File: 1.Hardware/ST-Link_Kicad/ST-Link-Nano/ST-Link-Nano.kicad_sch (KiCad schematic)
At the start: 26 parts, among them J1 USB_C_Receptacle_USB2.0, J2 JUMP, J3 Conn_02x04_Top_Bottom, U1 XC6210B332MR, U2 STM32F103CBTx, Y1 8MHz

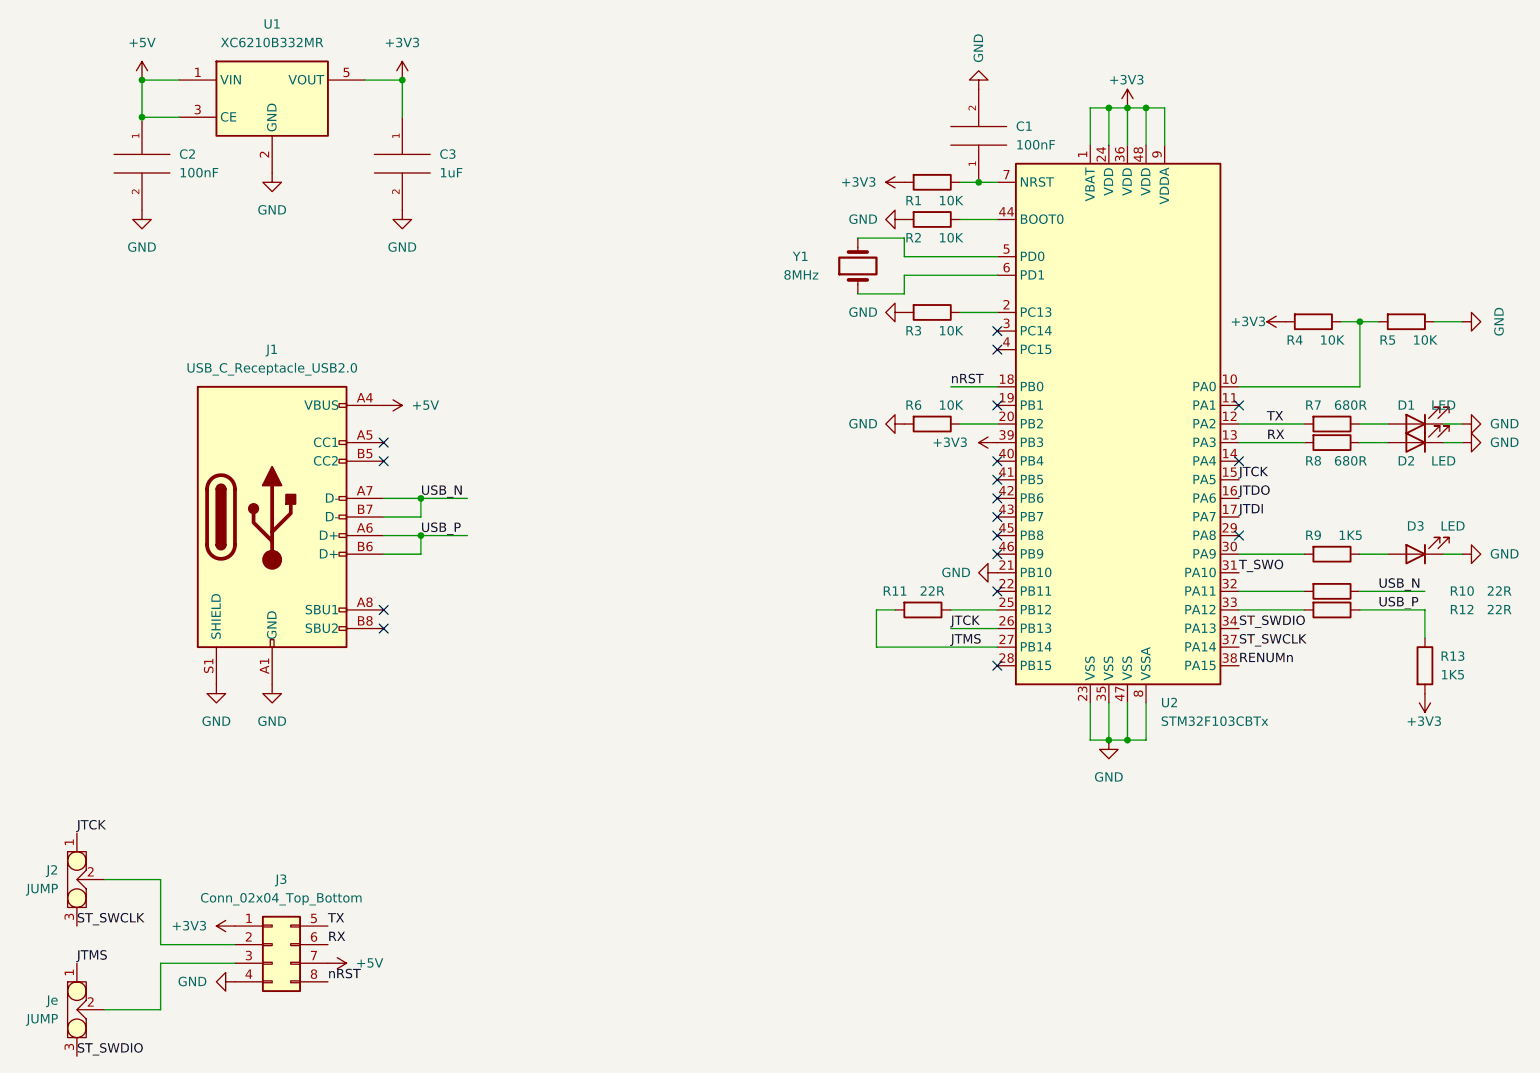
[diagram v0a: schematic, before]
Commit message: 在Kicad中画ST-Link的PCB，画到差不多一半
大概已经用了3～4小时，比想象中的要慢一些，第一次用Kicad画还不太熟
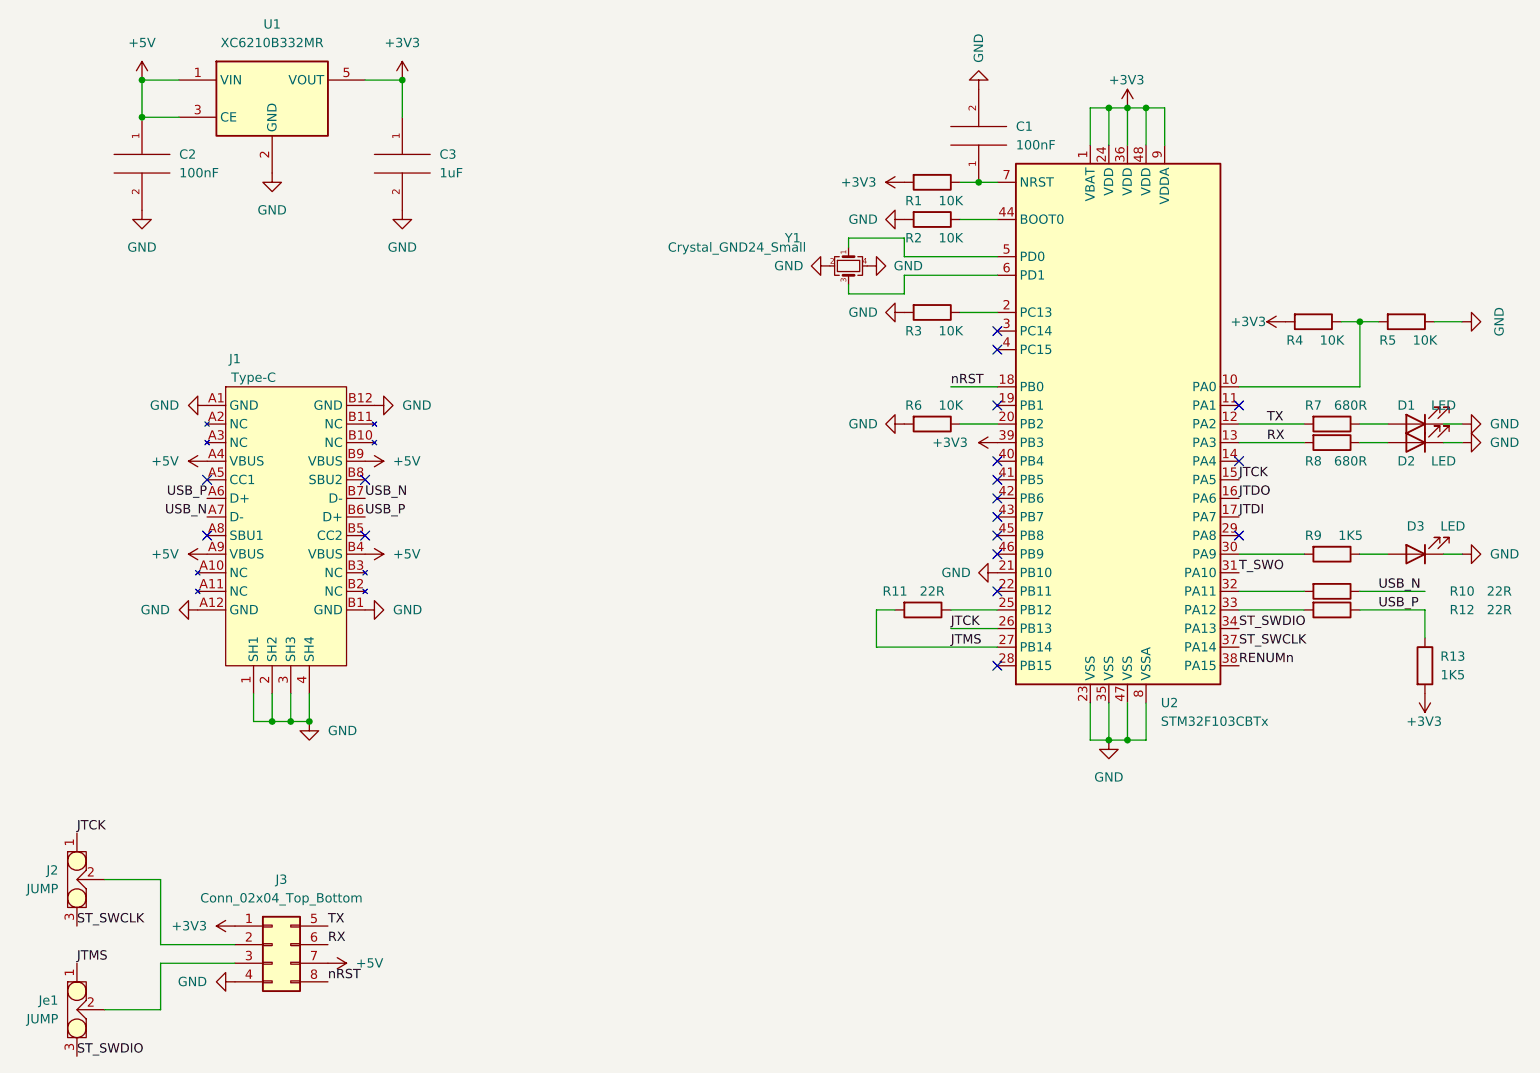
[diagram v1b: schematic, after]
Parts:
- removed J1: USB_C_Receptacle_USB2.0, symbol Connector:USB_C_Receptacle_USB2.0
- removed Y1: 8MHz, symbol Device:Crystal
- added J1: Type-C, MyLibrary:TYPE-CF-16P-RAT-L7.5W, symbol MyLibrary:Type-C
- added Y1: Crystal_GND24_Small, Crystal:Crystal_SMD_3225-4Pin_3.2x2.5mm, symbol Device:Crystal_GND24_Small
- renumbered Je to Je1
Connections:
- net +5V: now also J1.A4 (VBUS), J1.A9 (VBUS), J1.B4 (VBUS), J1.B9 (VBUS)
- net GND: now also J1.1 (SH1), J1.2 (SH2), J1.3 (SH3), J1.4 (SH4), J1.A1 (GND), J1.A12 (GND), J1.B1 (GND), J1.B12 (GND), Y1.2, Y1.4
- net USB_N: now also J1.A7 (D-), J1.B7 (D-)
- net USB_P: now also J1.A6 (D+), J1.B6 (D+)
- net at U2.5 (PD0): now also Y1.1
- net at U2.6 (PD1): now also Y1.3
